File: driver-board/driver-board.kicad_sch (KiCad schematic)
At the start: 25 parts, among them J1 MCP4725, J2 Conn_Coaxial, J3 MCP4725, SW1 RST, U1 Pico, U2 MIC5317, U3 TSV358, U4 TSV358, U5 TCBT-2R5G

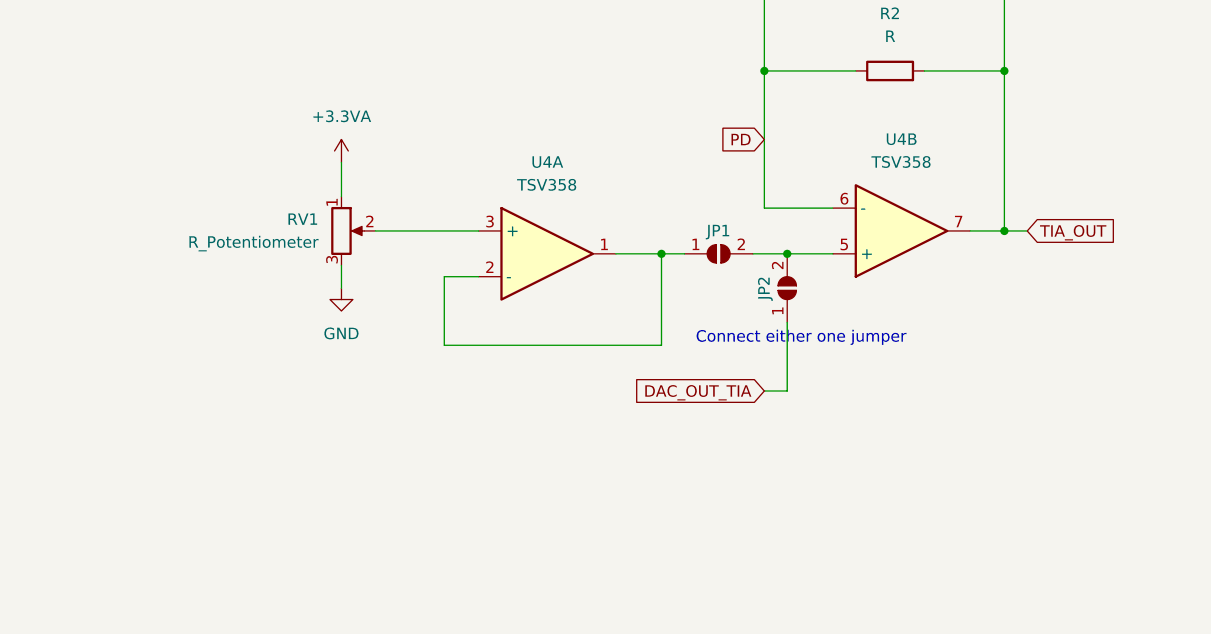
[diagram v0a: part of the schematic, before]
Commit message: fix pot footprint
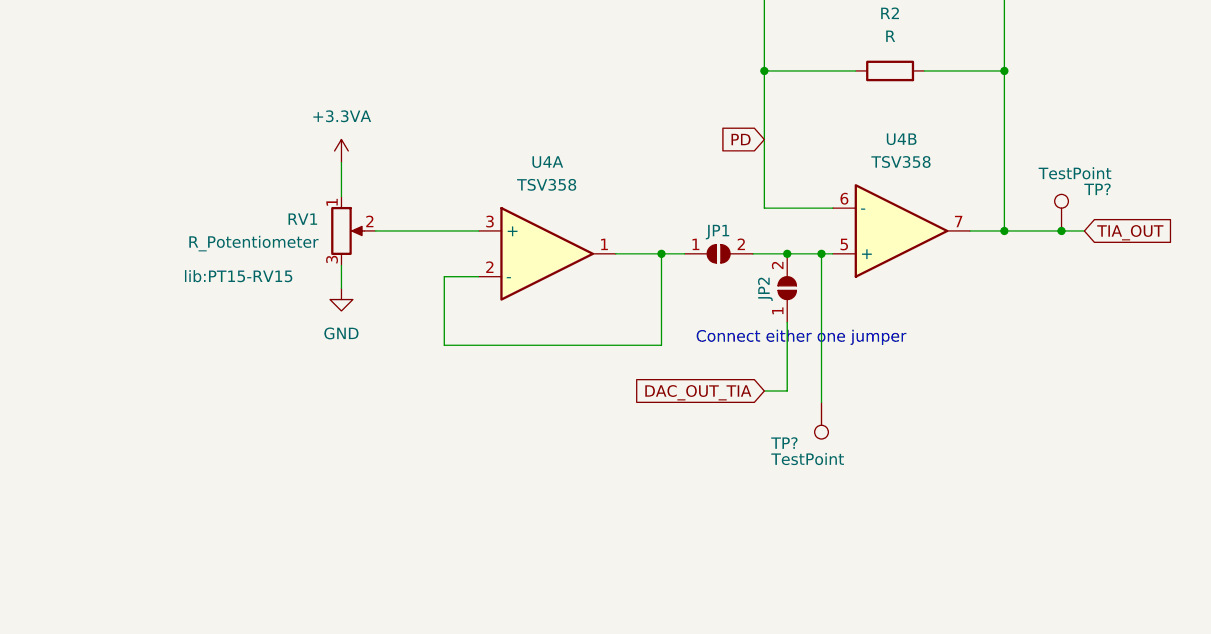
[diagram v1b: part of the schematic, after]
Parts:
- added TP? (x2): TestPoint, TestPoint:TestPoint_Pad_D2.0mm, symbol Connector:TestPoint
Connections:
- net TIA_OUT: now also TP?.1
- net at JP1.2 (B), JP2.2 (B), U4.5 (+): now also TP?.1
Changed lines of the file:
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@@
   (junction (at 113.03 95.25) (diameter 0) (color 0 0 0 0)
+  )
+  (junction (at 271.78 111.76) (diameter 0) (color 0 0 0 0)
+  )
+  (junction (at 245.11 114.3) (diameter 0) (color 0 0 0 0)
   )
   (junction (at 241.3 114.3) (diameter 0) (color 0 0 0 0)
@@
     (stroke (width 0) (type default) (color 0 0 0 0))
   )
+  (wire (pts (xy 271.78 111.76) (xy 274.32 111.76))
+    (stroke (width 0) (type default) (color 0 0 0 0))
+  )
   (wire (pts (xy 227.33 114.3) (xy 222.25 114.3))
     (stroke (width 0) (type default) (color 0 0 0 0))
@@
     (stroke (width 0) (type default) (color 0 0 0 0))
   )
-  (wire (pts (xy 246.38 114.3) (xy 241.3 114.3))
+  (wire (pts (xy 246.38 114.3) (xy 245.11 114.3))
     (stroke (width 0) (type default) (color 0 0 0 0))
   )
@@
     (stroke (width 0) (type default) (color 0 0 0 0))
   )
+  (wire (pts (xy 245.11 114.3) (xy 241.3 114.3))
+    (stroke (width 0) (type default) (color 0 0 0 0))
+  )
   (wire (pts (xy 149.86 83.82) (xy 149.86 80.01))
     (stroke (width 0) (type default) (color 0 0 0 0))
@@
     (stroke (width 0) (type default) (color 0 0 0 0))
   )
-  (wire (pts (xy 265.43 111.76) (xy 267.97 111.76))
+  (wire (pts (xy 265.43 111.76) (xy 271.78 111.76))
     (stroke (width 0) (type default) (color 0 0 0 0))
   )
@@
   )
   (wire (pts (xy 66.04 29.21) (xy 66.04 33.02))
+    (stroke (width 0) (type default) (color 0 0 0 0))
+  )
+  (wire (pts (xy 245.11 114.3) (xy 245.11 130.81))
     (stroke (width 0) (type default) (color 0 0 0 0))
   )
@@
     )
   )
-  (global_label "TIA_OUT" (shape input) (at 267.97 111.76 0) (fields_autoplaced)
-    (effects (font (size 1.27 1.27)) (justify left))
-    (property "Intersheet References" "${INTERSHEET_REFS}" (id 0) (at 277.6402 111.6806 0)
+  (global_label "TIA_OUT" (shape input) (at 274.32 111.76 0) (fields_autoplaced)
+    (effects (font (size 1.27 1.27)) (justify left))
+    (property "Intersheet References" "${INTERSHEET_REFS}" (id 0) (at 283.9902 111.6806 0)
       (effects (font (size 1.27 1.27)) (justify left) hide)
     )
@@
   )
   (symbol (lib_id "Device:R_Potentiometer") (at 191.77 111.76 0) (unit 1)
-    (in_bom yes) (on_board yes) (fields_autoplaced)
+    (in_bom yes) (on_board yes)
     (property "Reference" "RV1" (id 0) (at 189.23 110.4899 0)
       (effects (font (size 1.27 1.27)) (justify right))
@@
       (effects (font (size 1.27 1.27)) (justify right))
     )
-    (property "Footprint" "lib:PT15-RV15" (id 2) (at 191.77 111.76 0)
-      (effects (font (size 1.27 1.27)) hide)
-    )
+    (property "Footprint" "lib:PT15-RV15" (id 2) (at 180.34 116.84 0))
     (property "Datasheet" "~" (id 3) (at 191.77 111.76 0)
       (effects (font (size 1.27 1.27)) hide)
@@
     (pin "1")
   )
+  (symbol (lib_id "Connector:TestPoint") (at 271.78 111.76 0) (unit 1)
+    (in_bom yes) (on_board yes)
+    (property "Reference" "TP?" (id 0) (at 274.32 107.1879 0)
+      (effects (font (size 1.27 1.27)) (justify left))
+    )
+    (property "Value" "TestPoint" (id 1) (at 269.24 105.41 0)
+      (effects (font (size 1.27 1.27)) (justify left))
+    )
+    (property "Footprint" "TestPoint:TestPoint_Pad_D2.0mm" (id 2) (at 276.86 111.76 0)
+      (effects (font (size 1.27 1.27)) hide)
+    )
+    (property "Datasheet" "~" (id 3) (at 276.86 111.76 0)
+      (effects (font (size 1.27 1.27)) hide)
+    )
+    (pin "1")
+  )
   (symbol (lib_id "fd-fnir:TSV358") (at 97.79 38.1 0) (unit 3)
     (in_bom yes) (on_board yes) (fields_autoplaced)
@@
     (pin "8")
   )
+  (symbol (lib_id "Connector:TestPoint") (at 245.11 130.81 180) (unit 1)
+    (in_bom yes) (on_board yes)
+    (property "Reference" "TP?" (id 0) (at 242.57 135.3821 0)
+      (effects (font (size 1.27 1.27)) (justify left))
+    )
+    (property "Value" "TestPoint" (id 1) (at 247.65 137.16 0)
+      (effects (font (size 1.27 1.27)) (justify left))
+    )
+    (property "Footprint" "TestPoint:TestPoint_Pad_D2.0mm" (id 2) (at 240.03 130.81 0)
+      (effects (font (size 1.27 1.27)) hide)
+    )
+    (property "Datasheet" "~" (id 3) (at 240.03 130.81 0)
+      (effects (font (size 1.27 1.27)) hide)
+    )
+    (pin "1")
+  )
   (symbol (lib_id "Connector:Conn_01x06_Female") (at 24.13 86.36 0) (mirror y) (unit 1)
     (in_bom yes) (on_board yes) (fields_autoplaced)
@@
       (reference "TP2") (unit 1) (value "TestPoint") (footprint "TestPoint:TestPoint_Pad_D2.0mm")
     )
+    (path "/615ff202-7383-4031-83f4-9f2463dbc12a"
+      (reference "TP?") (unit 1) (value "TestPoint") (footprint "TestPoint:TestPoint_Pad_D2.0mm")
+    )
+    (path "/cee34a43-b4c9-4a9e-84b4-1fc8fae03e8e"
+      (reference "TP?") (unit 1) (value "TestPoint") (footprint "TestPoint:TestPoint_Pad_D2.0mm")
+    )
     (path "/3193b6ac-f0ad-4e05-b371-42ddbe4929f0"

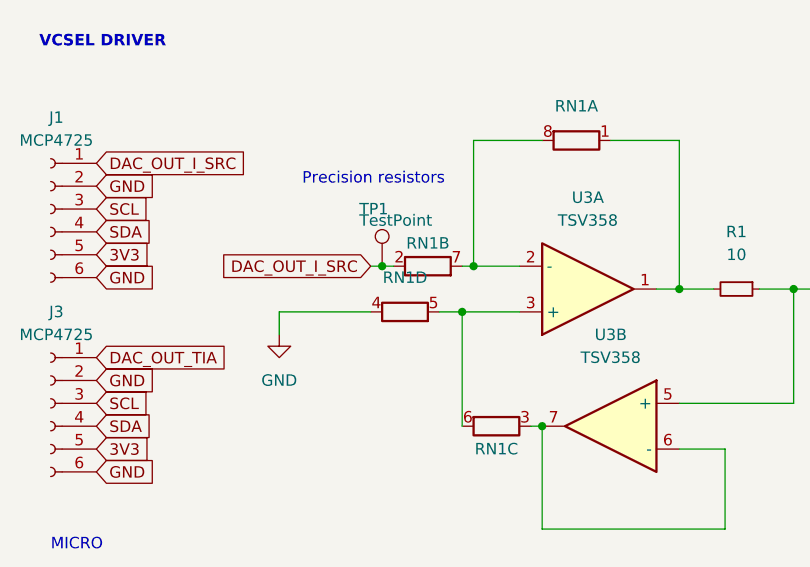
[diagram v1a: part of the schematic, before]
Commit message: more test points and design rules
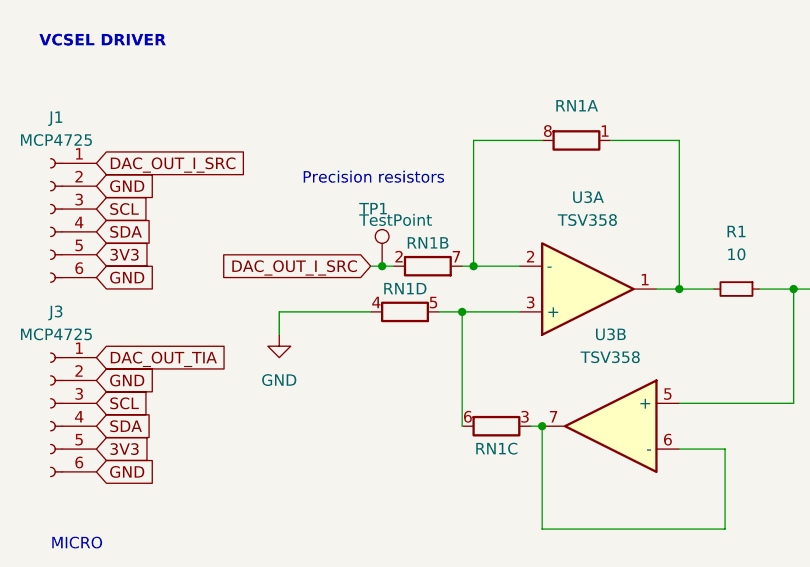
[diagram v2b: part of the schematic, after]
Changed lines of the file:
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@@
   )
   (symbol (lib_id "fd-fnir:R_Pack04_SIP_Split") (at 63.5 97.79 270) (unit 4)
-    (in_bom yes) (on_board yes) (fields_autoplaced)
-    (property "Reference" "RN1" (id 0) (at 63.5 93.98 90))
+    (in_bom yes) (on_board yes)
+    (property "Reference" "RN1" (id 0) (at 63.5 95.25 90))
     (property "Value" "R_Pack04_SIP_Split" (id 1) (at 63.5 101.6 90)
       (effects (font (size 1.27 1.27)) hide)

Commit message: temp
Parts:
- added C10: 0.01u, symbol Device:C_Small
- added C11: 0.1u, symbol Device:C_Small
- added C12: 100u, symbol Device:C_Small
- added C8, C9: 0, Capacitor_SMD:C_0805_2012Metric_Pad1.18x1.45mm_HandSolder, symbol Device:C_Small
- added J4, J5: Conn_01x06_Male, Connector_PinHeader_2.54mm:PinHeader_1x06_P2.54mm_Vertical, symbol Connector:Conn_01x06_Male
- added J6: MAX5026_O, symbol Connector:Conn_01x02_Male
- added J8: MAX5026, symbol Connector:Conn_01x02_Male
- added JP3: SolderJumper_2_Open, Jumper:SolderJumper-2_P1.3mm_Open_RoundedPad1.0x1.5mm, symbol Jumper:SolderJumper_2_Open
- added R3: 1k, symbol Device:R_Small
- added RV2: 100K, symbol Device:R_Potentiometer
- added U6: LM2904, symbol Amplifier_Operational:LM2904
- TP1, TP2: footprint TestPoint:TestPoint_Pad_D2.0mm -> TestPoint:TestPoint_Pad_D1.5mm
- TP3, TP4: renamed from TP?; footprint TestPoint:TestPoint_Pad_D2.0mm -> TestPoint:TestPoint_Pad_D1.5mm
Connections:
- net +3.3VA: now also C8.1, C9.1; no longer U1.35 (ADC_VREF)
- net 5V: now also J4.1 (Pin_1), J5.1 (Pin_1)
- net DAC_OUT_I_SRC: now also J4.3 (Pin_3), J5.3 (Pin_3)
- net DAC_OUT_TIA: now also J4.4 (Pin_4), J5.4 (Pin_4)
- net GND: now also C8.2, C9.2, J4.2 (Pin_2), J4.5 (Pin_5), J5.2 (Pin_2), J5.5 (Pin_5)
- net TIA_OUT: now also J4.6 (Pin_6), J5.6 (Pin_6)
- net at RV1.2: now also JP3.1 (A); no longer U4.3 (+)
- net SDA1: now reaches U1.6 (GPIO4)
- net SDA1: now also J3.4 (Pin_4)
- net SCL1: now reaches U1.7 (GPIO5)
- net SCL1: now also J3.3 (Pin_3)
- net SCL renamed SCL0
- net SCL0: no longer J3.3 (Pin_3)
- net SDA renamed SDA0
- net SDA0: no longer J3.4 (Pin_4)
- new net: C10.2, RV2.2, U6.3 (+)
- new net: JP3.2 (B), U4.3 (+)
- new net +33V: J6.1 (Pin_1), RV2.1
- new net 33V: U6.8 (V+)
- new net HV_GND: C10.1, C11.1, C12.1, J6.2 (Pin_2), J8.2 (Pin_2), R3.2, RV2.3, U6.1, U6.2 (-), U6.4 (V-)
- new net SiPM Bias: C11.2, C12.2, J8.1 (Pin_1), R3.1
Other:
- note added: "SiPM BIAS"
- note added: "Wavelength @ 500MHz = 300mm Max via stitch spacing = 300/20 = 15mm"
- moved on the sheet: C3, C4, LD1, U3C, U4C

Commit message: Anything
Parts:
- removed J6: MAX5026_O, symbol Connector:Conn_01x02_Male
- added C, C? (x2): 1u, Capacitor_SMD:C_0805_2012Metric_Pad1.18x1.45mm_HandSolder, symbol Device:C_Small
- added C?: 22p, Capacitor_SMD:C_0805_2012Metric_Pad1.18x1.45mm_HandSolder, symbol Device:C_Small
- added L? (x2): 22u, symbol Device:L
- added R?: 470k, symbol Device:R_Small
- added R?: 18k, symbol Device:R_Small
- added U?: LT3462A, symbol fd-fnir:LT3462A
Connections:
- net +33V is gone; now on net GND: RV2.1
- net 33V is gone; now on net GND: U6.8 (V+)
- net 5V: now also C?.2, L?.1, U?.6 (VIN)
- net GND: now also J8.2 (Pin_2), C.1, C?.1, U?.GND (2)
- net HV_GND renamed -33V
- net -33V: now also C.2, C?.2, L?.2, R?.2; no longer J8.2 (Pin_2)
- new net: C?.1, R?.1, R?.2, U?.3 (FB)
- new net: C?.1, L?.2, U?.1 (SW)
- new net: R?.1, U?.4 (SDREF)
- new net: C?.2, L?.1, U?.5 (D)
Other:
- note added: "MONITOR PD TRANSIMPEDANCE AMPLIFIER"

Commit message: Passing DRC
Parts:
- removed J4, J5: Conn_01x06_Male, Connector_PinHeader_2.54mm:PinHeader_1x06_P2.54mm_Vertical, symbol Connector:Conn_01x06_Male
- removed J8: MAX5026, symbol Connector:Conn_01x02_Male
- removed JP2, JP3: SolderJumper_2_Open, Jumper:SolderJumper-2_P1.3mm_Open_RoundedPad1.0x1.5mm, symbol Jumper:SolderJumper_2_Open
- removed RV1: R_Potentiometer, lib:PT15-RV15, symbol Device:R_Potentiometer
- removed unit 1 of U4
- added J4: Conn_Coaxial, lib:CONSMA020.062-G, symbol Connector:Conn_Coaxial
- added R6, R7, R8: 0, Resistor_SMD:R_0805_2012Metric_Pad1.20x1.40mm_HandSolder, symbol Device:R_Small
- added SW2: SW_DPDT_x2, lib:JS202011SCQN, symbol Switch:SW_DPDT_x2
- added TP5, TP6, TP7: TestPoint, TestPoint:TestPoint_Pad_D1.5mm, symbol Connector:TestPoint
- added unit 2 of U6
- C10, C11: footprint (none) -> Capacitor_SMD:C_0805_2012Metric_Pad1.18x1.45mm_HandSolder
- C12: footprint (none) -> Capacitor_THT:CP_Radial_D10.0mm_P3.50mm
- JP1: footprint Jumper:SolderJumper-2_P1.3mm_Open_RoundedPad1.0x1.5mm -> Jumper:SolderJumper-2_P1.3mm_Bridged_Pad1.0x1.5mm; symbol Jumper:SolderJumper_2_Open -> Jumper:SolderJumper_2_Bridged
- L1, L2: renamed from L?; footprint (none) -> Inductor_SMD:L_1210_3225Metric_Pad1.42x2.65mm_HandSolder
- R3: footprint (none) -> Resistor_SMD:R_0805_2012Metric_Pad1.20x1.40mm_HandSolder
- R4, R5: renamed from R?; footprint (none) -> Resistor_SMD:R_0805_2012Metric_Pad1.20x1.40mm_HandSolder
- RV2: footprint (none) -> lib:PT15-RV15
- U1: footprint lib:RPi_Pico_SMD_TH -> lib:RPi_Pico_minimal; symbol fd-fnir:Pico -> fd-fnir:Pico_minimal
- U6: footprint (none) -> Package_SO:TSSOP-8_4.4x3mm_P0.65mm
- U7: renamed from U?; footprint (none) -> Package_TO_SOT_SMD:TSOT-23-6
- gave numbers to parts that had none: 3
- renumbered C to C16
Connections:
- net -33V: no longer C10.1, C11.1, C12.1, R3.2, U6.1, U6.2 (-)
- net DAC_OUT_TIA: now also JP1.1 (A)
- net GND: now also C10.1, C11.1, C12.1, R3.2, U6.1, U6.2 (-), U7.2 (GND), J4.2 (Ext), SW2.3 (C); no longer U7.GND (2)
- net SiPM Bias: now also J4.1 (In)
- net at C10.2, U6.3 (+): now also SW2.2 (B); no longer RV2.2
- new net: R6.2, TP5.1
- new net: R8.1, TP7.1, U6.7
- new net: R6.1, R8.2, U6.6 (-)
- new net: RV2.2, SW2.1 (A)
- new net: R7.1, U6.5 (+)
- new net: R7.2, TP6.1
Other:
- note removed: "Connect either one jumper"
- moved on the sheet: C10, C11, C12, C13, C14, C15, C16, C6, C7, L1, L2, LD1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

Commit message: DRC passing, updated HV section and mounting
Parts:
- added unit 1 of U4
- SW2: value SW_DPDT_x2 -> BIAS ON/OF
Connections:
- net GND: now also C10.2, U6.3 (+); no longer C10.1, R3.2, U6.1, U6.2 (-)
- new net: C10.1, R3.2, SW2.2 (B), U6.1, U6.2 (-)
- no-connect marks 1 -> 4
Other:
- moved on the sheet: C10, R6, R7, R8, RV2, TP5, TP6, TP7, U6B
